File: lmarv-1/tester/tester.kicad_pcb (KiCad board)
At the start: 4 copper layers, 145 x 59.4 mm, 88 parts, among them P1 dual-pcie-cardedge, U1 74HC597, U10 74HC597, U11 74HC597, U12 74HC597, U13 74LVC595, U14 74LVC595, U15 74LVC595, U16 74LVC595, U17 74HC597, U18 74HC597, U19 74HC597, U2 74HC597, U20 74HC597, U21 TinyFPGA_BX, U22 74LVC595, U23 74LVC595, U24 74LVC595, U25 74LVC595, U26 74HC597, U27 74HC597, U28 74HC597, U29 74HC597, U3 74HC597, U30 74LVC595, U31 74LVC595, U32 74LVC595, U33 74LVC595, U34 74HC597, U35 74HC597, U36 74HC597, U37 74HC597, U38 74LVC595, U39 74LVC595, U4 74HC597, U40 74LVC595, U41 74LVC595, U5 74LVC595, U6 74LVC595, U7 74LVC595, U8 74LVC595, U9 74HC597

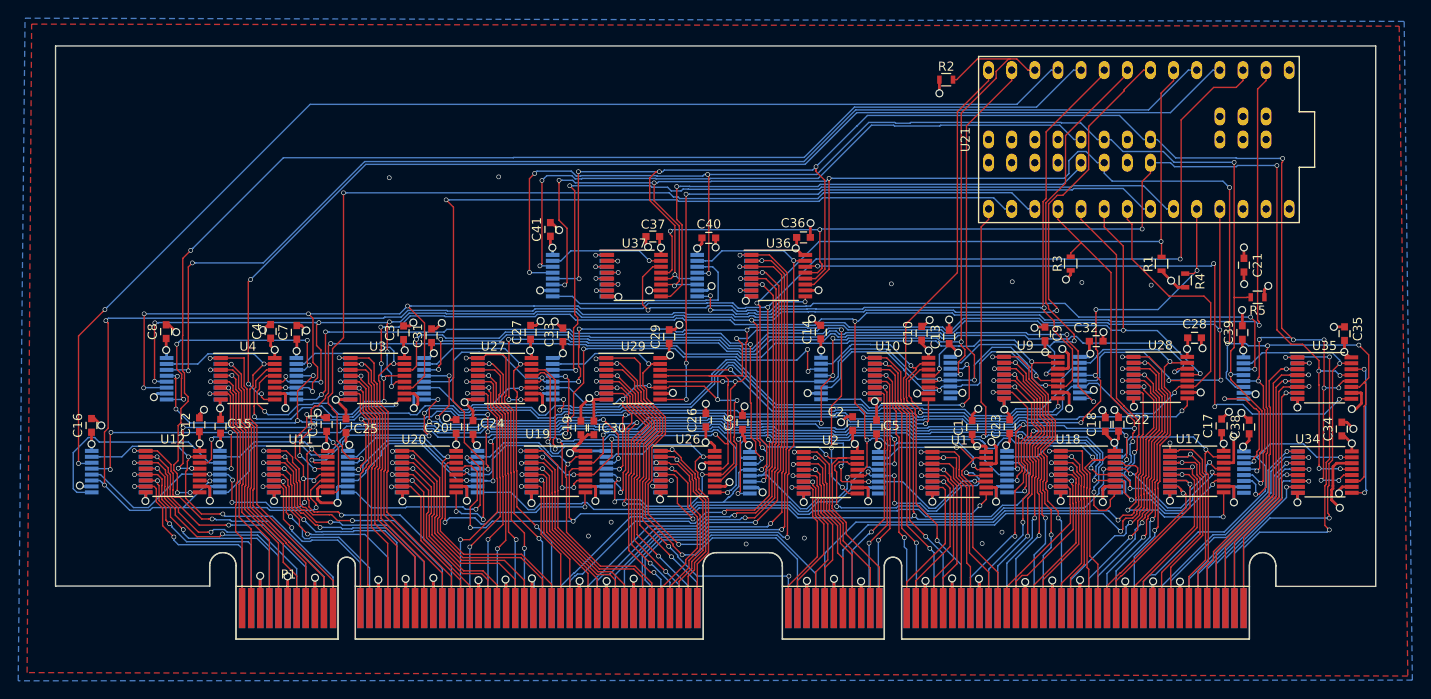
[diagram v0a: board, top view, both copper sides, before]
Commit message: Mainly updates alu.py simulator
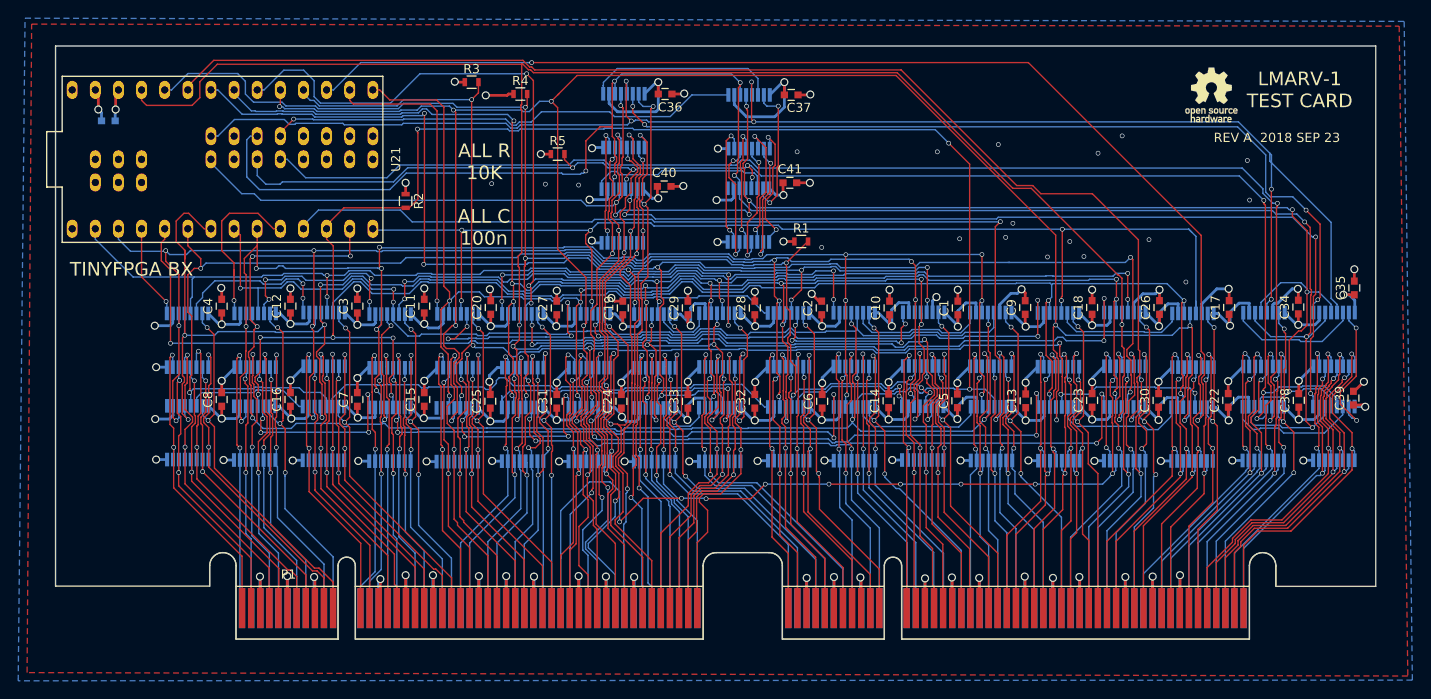
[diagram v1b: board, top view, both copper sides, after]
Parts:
- added REF***: OSHW-Logo_5.7x6mm_SilkScreen, Symbols:OSHW-Logo_5.7x6mm_SilkScreen, F.Cu at (176.9, 91.0)
- C21, U1, U10, U11, U12, U17, U18, U19, U2, U20, U26, U27, U28, U29, U3, U34, U35, U36, U37, U4, U9: moved to B.Cu
- moved C21 125.7 mm to (55.8, 93.8), turned to 180 degrees
- moved U21 100.7 mm to (68.3, 98.0), turned to 0 degrees
- moved R5 78.5 mm to (105.2, 97.5), turned to 0 degrees
- moved R4 75.8 mm to (101.0, 90.8), turned to 0 degrees
- moved R3 68.8 mm to (95.7, 89.5), turned to 0 degrees
- moved C30 62.1 mm to (171.2, 124.5)
- moved R2 60.9 mm to (88.5, 102.6), turned to 270 degrees
- moved U30 54.1 mm to (167.4, 128.2), turned to 90 degrees
- moved C26 51.3 mm to (171.2, 114.3)
- moved U26 50.1 mm to (167.4, 117.8), turned to 90 degrees
- moved U28 48.6 mm to (123.0, 117.9), turned to 90 degrees
- moved C28 48.4 mm to (126.8, 114.3), turned to 90 degrees
- moved U32 43.0 mm to (123.0, 128.2), turned to 90 degrees
- moved R1 39.7 mm to (131.9, 107.0), turned to 0 degrees
- moved C32 38.1 mm to (126.8, 124.6), turned to 90 degrees
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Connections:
- U13 pad 14: /RS1WS0 -> /RS1SI
- U13 pad 9: Net-(U13-Pad9) -> /RS1WS0
- U14 pad 14: /RS1WS1 -> /RS1WS0
- U14 pad 9: /RS1WS0 -> /RS1WS1
- U15 pad 14: /RS1WS2 -> /RS1WS1
- U15 pad 9: /RS1WS1 -> /RS1WS2
- U16 pad 14: /RS1SI -> /RS1WS2
- U16 pad 9: /RS1WS2 -> Net-(U16-Pad9)
- U21 pad 26: Net-(U21-Pad26) -> VCC
- U22 pad 14: /RS2WS0 -> /RS2SI
- U22 pad 9: Net-(U22-Pad9) -> /RS2WS0
- U23 pad 14: /RS2WS1 -> /RS2WS0
- U23 pad 9: /RS2WS0 -> /RS2WS1
- U24 pad 14: /RS2WS2 -> /RS2WS1
- U24 pad 9: /RS2WS1 -> /RS2WS2
- U25 pad 14: /RS2SI -> /RS2WS2
- U25 pad 9: /RS2WS2 -> Net-(U25-Pad9)
- U26 pad 1: /rda[3] -> /~rs1_blh
- U26 pad 15: /rda[4] -> /~rs1_bll
- U26 pad 2: /rda[2] -> /~rs2_bll
- U26 pad 3: /rda[1] -> /~rs2_blh
- U26 pad 4: /rda[0] -> /~rd_bll
- U26 pad 5: /~rs1_rd -> /~rd_blh
- U26 pad 6: /q0 -> /~rs1_rd
- U26 pad 7: /q1 -> /q0
- U28 pad 1: /~rs1_blh -> /rda[4]
- U28 pad 15: /~rs1_bll -> /q1
- U28 pad 2: /~rs2_bll -> /rda[3]
- U28 pad 3: /~rs2_blh -> /rda[2]
- U28 pad 4: /~rd_bll -> /rda[1]
- U28 pad 5: /~rd_blh -> /rda[0]
- U30 pad 1: /rda[3] -> /~rs1_blh
- U30 pad 14: /RCWS0 -> /RCSI
- U30 pad 15: /rda[4] -> /~rs1_bll
- U30 pad 2: /rda[2] -> /~rs2_bll
- U30 pad 3: /rda[1] -> /~rs2_blh
- U30 pad 4: /rda[0] -> /~rd_bll
- U30 pad 5: /~rs1_rd -> /~rd_blh
- U30 pad 6: /q0 -> /~rs1_rd
- U30 pad 7: /q1 -> /q0
- U30 pad 9: Net-(U30-Pad9) -> /RCWS0
- U31 pad 14: /RCWS1 -> /RCWS0
- U31 pad 9: /RCWS0 -> /RCWS1
- U32 pad 1: /~rs1_blh -> /rda[4]
- U32 pad 14: /RCWS2 -> /RCWS1
- U32 pad 15: /~rs1_bll -> /q1
- U32 pad 2: /~rs2_bll -> /rda[3]
- U32 pad 3: /~rs2_blh -> /rda[2]
- U32 pad 4: /~rd_bll -> /rda[1]
- U32 pad 5: /~rd_blh -> /rda[0]
- U32 pad 9: /RCWS1 -> /RCWS2
- U33 pad 14: /RCSI -> /RCWS2
- U33 pad 9: /RCWS2 -> Net-(U33-Pad9)
- U34 pad 1: /~alu_oe -> /~BOOT_ALU_EN
- U34 pad 15: /~shift_oe -> /BOOT_CLK
- U34 pad 2: /f[0] -> /f[3]
- U34 pad 3: /f[1] -> /f[2]
- U34 pad 4: /f[2] -> /f[1]
- U34 pad 5: /f[3] -> /f[0]
- U34 pad 6: /~BOOT_ALU_EN -> /~alu_oe
- U34 pad 7: /BOOT_CLK -> /~shift_oe
- U35 pad 1: /~BOOT_WR -> /nc[11]
- U35 pad 15: /~BOOT_RST -> /q2
- U35 pad 2: /q2 -> /nc[10]
- U35 pad 3: /nc[7] -> /nc[9]
- U35 pad 5: /nc[9] -> /nc[7]
- U35 pad 6: /nc[10] -> /~BOOT_WR
- U35 pad 7: /nc[11] -> /~BOOT_RST
- U38 pad 1: /~alu_oe -> /~BOOT_ALU_EN
- U38 pad 14: /CWS0 -> /CSI
- U38 pad 15: /~shift_oe -> /BOOT_CLK
- U38 pad 2: /f[0] -> /f[3]
- U38 pad 3: /f[1] -> /f[2]
- U38 pad 4: /f[2] -> /f[1]
- U38 pad 5: /f[3] -> /f[0]
- U38 pad 6: /~BOOT_ALU_EN -> /~alu_oe
- U38 pad 7: /BOOT_CLK -> /~shift_oe
- U38 pad 9: Net-(U38-Pad9) -> /CWS0
- U39 pad 1: /~BOOT_WR -> /nc[11]
- U39 pad 14: /CWS1 -> /CWS0
- U39 pad 15: /~BOOT_RST -> /q2
- U39 pad 2: /q2 -> /nc[10]
- U39 pad 3: /nc[7] -> /nc[9]
- U39 pad 5: /nc[9] -> /nc[7]
- U39 pad 6: /nc[10] -> /~BOOT_WR
- U39 pad 7: /nc[11] -> /~BOOT_RST
- U39 pad 9: /CWS0 -> /CWS1
- U40 pad 14: /CWS2 -> /CWS1
- U40 pad 9: /CWS1 -> /CWS2
- U41 pad 14: /CSI -> /CWS2
- U41 pad 9: /CWS2 -> Net-(U41-Pad9)
- U5 pad 14: /RDWS0 -> /RDSI
- U5 pad 9: Net-(U5-Pad9) -> /RDWS0
- U6 pad 14: /RDWS1 -> /RDWS0
- U6 pad 9: /RDWS0 -> /RDWS1
- U7 pad 14: /RDWS2 -> /RDWS1
- U7 pad 9: /RDWS1 -> /RDWS2
- U8 pad 14: /RDSI -> /RDWS2
- U8 pad 9: /RDWS2 -> Net-(U8-Pad9)
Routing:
- net /RDSO: track 131.4 -> 10.4 mm, vias 3 -> 1
- net /RS1SO: track 136.5 -> 18.8 mm, vias 3 -> 1
- net VCC: track 253.6 -> 360.0 mm, vias 80 -> 58
- net /~RDRLD: track 191.8 -> 115.4 mm, vias 9 -> 6
- net /RS2WLD: track 158.5 -> 231.0 mm, vias 7 -> 11
- net /RS2SO: track 105.2 -> 33.5 mm, vias 3 -> 1
- net /RS1CLK: track 237.6 -> 166.8 mm, vias 7 -> 13
- net /CSI: track 73.7 -> 140.0 mm
- net /~rs1_rd: track 28.3 -> 93.0 mm, vias 2 -> 10
- net /~RS1RLD: track 167.6 -> 104.7 mm, vias 10 -> 3
- net /RCWS2: track 68.0 -> 6.90 mm, vias 2 -> 0
- net /~RCOE: track 131.5 -> 189.7 mm, vias 10 -> 7
- net /RDCLK: track 229.7 -> 171.8 mm, vias 13 -> 12
- net /~RDOE: track 199.9 -> 142.7 mm, vias 9 -> 6
- net /RCRS2: track 62.4 -> 6.91 mm, vias 2 -> 0
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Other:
- net class Power: clearance 0.2032 -> 0.1524
- board text added: "74HC597"
- board text added: "74LVC595"
- board text added: "ALL C 100n"
- board text added: "ALL R 10K"
- board text added: "LMARV-1 TEST CARD"
- board text added: "REV A 2018 SEP 23"
- board text added: "TINYFPGA BX"
